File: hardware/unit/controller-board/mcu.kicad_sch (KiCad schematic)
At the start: 26 parts, among them U11 LP2985-33, U12 TPS3823A-33, U13 74LVC1G74, U14 74LVC1G27, U15 74LVC1G02

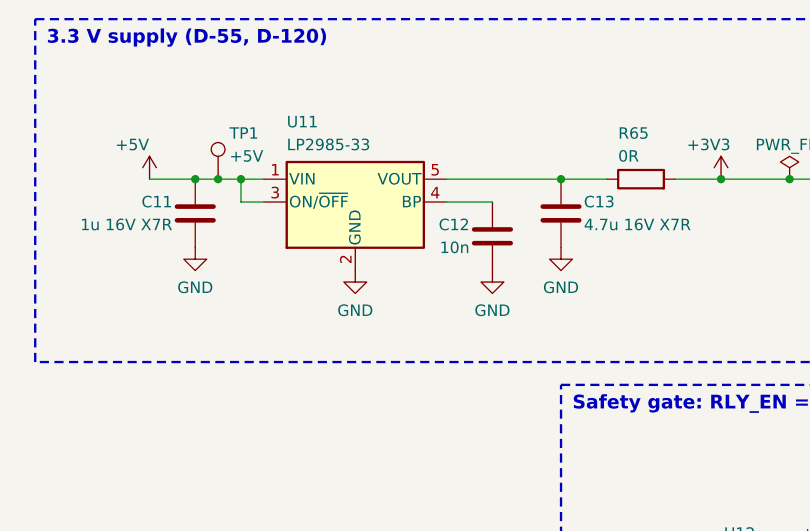
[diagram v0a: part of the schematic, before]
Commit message: Pre-order review; RF board seat keep-outs; part reuse P-1 to P-5
- docs/reviews/2026-10-31-pre-order-review.md: review of all three boards
  before ordering (verify scripts, ERC/DRC, pin maps, BOM, fab and case,
  firmware against spec, open items, part reuse).
- RF board (D-189, M-107): no other-net copper or vias under the case
  seats at S1 to S6 and the SO-239/SMA GND bosses; relay NC pads (pad 12)
  in netclass RF. Re-routed, DRC 0.
- Part reuse (D-190, M-108): one value text for 2k2, 100n 50V X7R and
  10n 50V X7R; shack PC817X order code as the controller; shack U4/U9 in
  VSSOP-8 (TI DCU, Nexperia DC) with fixed fan-out, re-routed.
  Netlists rf15, ctl15, si17; ERC 0.

Co-Authored-By: Claude Opus 5.5 <noreply@anthropic.com>
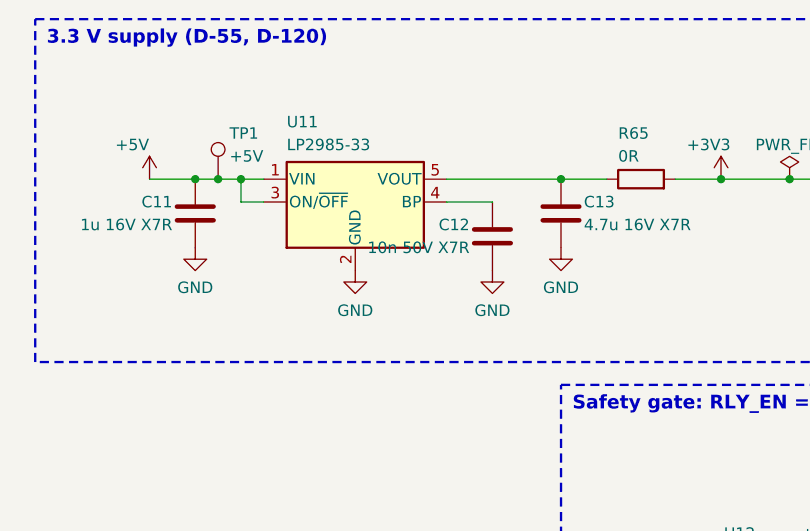
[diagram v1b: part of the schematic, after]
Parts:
- C12: value 10n -> 10n 50V X7R
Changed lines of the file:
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@@
 			)
 		)
-		(property "Value" "10n"
+		(property "Value" "10n 50V X7R"
 			(at 73.66 50.8 0)
 			(show_name no)

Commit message: S-1: FAULT to GPIO6, box fault 11, host clearfault
Hardware (D-191, M-109):
- Controller board: R66 1k from FAULT (U13 Q) to DevKit pin 11 (GPIO6).
  Schematic c15-fault-io6, netlist ctl16, layout c-s6, re-routed.
  ERC 0, DRC 0 violations and 0 unconnected. BOM: R66 on the 1k line.
- gen_controller_pcb.py splits a track where a same-net track ends on it.
- verify_logic.py checks R66 and FAULT_IO6.

Firmware:
- Box reads FAULT. After the self-test, FAULT = 1 gives fault 11
  (supervisor trip); READY stays open.
- New link command ClearFault (0x03): one LATCH_CLR edge, Ok if FAULT
  clears, else NotReady. No edge without a trip.
- Host clearfault also sends ClearFault when the box reports fault 11.
- Sim model, box target (GPIO6), 3 new tests.

Co-Authored-By: Claude Opus 5.5 <noreply@anthropic.com>
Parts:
- added R66: 1k, Resistor_SMD:R_0603_1608Metric_Pad0.98x0.95mm_HandSolder, symbol Device:R
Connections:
- net FAULT: now also R66.1
- net FAULT_IO6: now reaches A1.11 (IO6)
- net FAULT_IO6: now also R66.2
- no-connect marks 17 -> 16
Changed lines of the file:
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@@
 	)
 	(junction
+		(at 160.02 101.6)
+		(diameter 0)
+		(color 0 0 0 0)
+	)
+	(junction
 		(at 142.24 121.92)
 		(diameter 0)
@@
 		)
 	)
-	(no_connect
-		(at 43.18 190.5)
+	(wire
+		(pts
+			(xy 43.18 190.5) (xy 35.56 190.5)
+		)
+		(stroke
+			(width 0)
+			(type default)
+		)
+	)
+	(label "FAULT_IO6"
+		(at 35.56 190.5 180)
+		(effects
+			(font
+				(size 1.27 1.27)
+			)
+			(justify right bottom)
+		)
 	)
 	(wire
@@
 	(wire
 		(pts
-			(xy 160.02 93.98) (xy 160.02 119.38)
+			(xy 160.02 93.98) (xy 160.02 101.6)
+		)
+		(stroke
+			(width 0)
+			(type default)
+		)
+	)
+	(wire
+		(pts
+			(xy 160.02 101.6) (xy 160.02 119.38)
 		)
 		(stroke
@@
 	)
 	(symbol
+		(lib_id "Device:R")
+		(at 167.64 101.6 90)
+		(unit 1)
+		(body_style 1)
+		(exclude_from_sim no)
+		(in_bom yes)
+		(on_board yes)
+		(in_pos_files yes)
+		(dnp no)
+		(property "Reference" "R66"
+			(at 167.64 99.06 270)
+			(show_name no)
+			(do_not_autoplace no)
+			(effects
+				(font
+					(size 1.27 1.27)
+				)
+				(justify left)
+			)
+		)
+		(property "Value" "1k"
+			(at 167.64 101.6 270)
+			(show_name no)
+			(do_not_autoplace no)
+			(effects
+				(font
+					(size 1.27 1.27)
+				)
+				(justify left)
+			)
+		)
+		(property "Footprint" "Resistor_SMD:R_0603_1608Metric_Pad0.98x0.95mm_HandSolder"
+			(at 167.64 101.6 0)
+			(hide yes)
+			(show_name no)
+			(do_not_autoplace no)
+			(effects
+				(font
+					(size 1.27 1.27)
+				)
+				(justify left)
+			)
+		)
+		(property "Datasheet" ""
+			(at 167.64 101.6 0)
+			(hide yes)
+			(show_name no)
+			(do_not_autoplace no)
+			(effects
+				(font
+					(size 1.27 1.27)
+				)
+				(justify left)
+			)
+		)
+		(property "Description" "FAULT to GPIO6 (D-191): series resistor, the MCU reads the fault latch"
+			(at 167.64 101.6 0)
+			(hide yes)
+			(show_name no)
+			(do_not_autoplace no)
+			(effects
+				(font
+					(size 1.27 1.27)
+				)
+				(justify left)
+			)
+		)
+		(pin "1"
+		)
+		(pin "2"
+		)
+		(instances
+			(project "controller-board"
+				(path "/b86ecb39-90cb-58dd-93b8-afa48d7a2239/6efcfdd3-b192-5236-8b01-1f2c86853060"
+					(reference "R66")
+					(unit 1)
+				)
+			)
+		)
+	)
+	(wire
+		(pts
+			(xy 160.02 101.6) (xy 163.83 101.6)
+		)
+		(stroke
+			(width 0)
+			(type default)
+		)
+	)
+	(wire
+		(pts
+			(xy 171.45 101.6) (xy 177.8 101.6)
+		)
+		(stroke
+			(width 0)
+			(type default)
+		)
+	)
+	(label "FAULT_IO6"
+		(at 177.8 101.6 0)
+		(effects
+			(font
+				(size 1.27 1.27)
+			)
+			(justify left bottom)
+		)
+	)
+	(symbol
 		(lib_id "Connector:TestPoint")
 		(at 165.1 93.98 0)
@@
 		)
 	)
-	(text "MCU: ESP32-C3 Rust board A1 (DevKit-RUST-1 Rev 1.2a fitted, RUST-2 fits) in gold socket headers (D-93 to D-95). Net labels at the DevKit pins.\n3V3 pin from U11 (LDO); EN low keeps the board buck off;\n5V/VBUS not connected, so the PC can stay on USB (board diode D6). Wi-Fi and BLE off in firmware.\nI2C: board bus SDA GPIO10 (RUST-1) or GPIO7 (RUST-2), set by JP11 (2-3 or 2-1, D-94); SCL GPIO8. 10k on the board; 2.2k on the RF board.\nGPIO0 EXP_INT, GPIO1 WDI (kick at least every 0.9 s), GPIO3 LATCH_CLR (rising edge), GPIO4 MCU_EN_N (low = relays allowed),\nGPIO5 KILL (read), GPIO20/21 UART 9600 baud. GPIO2, 8, 9 are strapping pins: GPIO2 and GPIO9 not used; GPIO8 is SCL. GPIO6 spare.\nBoard LED on GPIO7 (RUST-1) or GPIO10 (RUST-2): the SDA pin of the other board.\nSafety gate (D-59): RLY_EN = NOR(KILL, MCU_EN_N, FAULT). FAULT is set by RESET_N: power-up, 3V3 below 2.83 to 3.00 V, or no WDI edge for 0.9 to 2.5 s.\nAfter a reset the relays stay off until the MCU gives a LATCH_CLR edge. KILL is not latched. RLY_EN has a 100k pull-down on the RF board.\nREADY_ON = NOR(MCU_EN_N, FAULT) (U15, D-62): closes the READY switch in the SAFE loop. Start-up: LATCH_CLR, MCU_EN_N low, then KILL reads 0 (F11).\nU12 RESET_N does not reset the MCU (DevKit pin 1 RST open); the ESP32-C3 has its own watchdogs. MR open: internal 90k pull-up."
+	(text "MCU: ESP32-C3 Rust board A1 (DevKit-RUST-1 Rev 1.2a fitted, RUST-2 fits) in gold socket headers (D-93 to D-95). Net labels at the DevKit pins.\n3V3 pin from U11 (LDO); EN low keeps the board buck off;\n5V/VBUS not connected, so the PC can stay on USB (board diode D6). Wi-Fi and BLE off in firmware.\nI2C: board bus SDA GPIO10 (RUST-1) or GPIO7 (RUST-2), set by JP11 (2-3 or 2-1, D-94); SCL GPIO8. 10k on the board; 2.2k on the RF board.\nGPIO0 EXP_INT, GPIO1 WDI (kick at least every 0.9 s), GPIO3 LATCH_CLR (rising edge), GPIO4 MCU_EN_N (low = relays allowed),\nGPIO5 KILL (read), GPIO6 FAULT (read, 1k R66, D-191), GPIO20/21 UART 9600 baud. GPIO2, 8, 9 are strapping pins: GPIO2 and GPIO9 not used; GPIO8 is SCL.\nBoard LED on GPIO7 (RUST-1) or GPIO10 (RUST-2): the SDA pin of the other board.\nSafety gate (D-59): RLY_EN = NOR(KILL, MCU_EN_N, FAULT). FAULT is set by RESET_N: power-up, 3V3 below 2.83 to 3.00 V, or no WDI edge for 0.9 to 2.5 s.\nAfter a reset the relays stay off until the MCU gives a LATCH_CLR edge. KILL is not latched. RLY_EN has a 100k pull-down on the RF board.\nREADY_ON = NOR(MCU_EN_N, FAULT) (U15, D-62): closes the READY switch in the SAFE loop. Start-up: LATCH_CLR, MCU_EN_N low, then KILL reads 0 (F11).\nU12 RESET_N does not reset the MCU (DevKit pin 1 RST open); the ESP32-C3 has its own watchdogs. MR open: internal 90k pull-up."
 		(exclude_from_sim no)
 		(at 25.4 223.52 0)

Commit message: S-2: SDA jumpers bridged 1-2 for RUST-1 by default
JP11 (controller) and JP61 (shack) use the Bridged12 solder jumper.
Pad 1 = SDA_IO10 (RUST-1), pad 3 = SDA_IO7 (RUST-2). Boards ship ready
for RUST-1; for RUST-2 cut 1-2 and bridge 2-3. New netlists ctl17 and
si18, new JP11/JP61 checks, boards re-routed, DRC clean. D-192, M-110.

Co-Authored-By: Claude Opus 5.5 <noreply@anthropic.com>
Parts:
- JP11: footprint Jumper:SolderJumper-3_P1.3mm_Open_RoundedPad1.0x1.5mm_NumberLabels -> Jumper:SolderJumper-3_P1.3mm_Bridged12_RoundedPad1.0x1.5mm_NumberLabels; symbol controller-board:SolderJumper_3_Open -> controller-board:SolderJumper_3_Bridged12
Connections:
- net SDA_IO10: now also JP11.1; no longer JP11.3
- net SDA_IO7: now also JP11.3; no longer JP11.1
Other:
- note added: "MCU: ESP32-C3 Rust board A1 (DevKit-RUST-1 Rev 1.2a fitted, RUST-2 fits) in gold socket headers (D-93 to D-95). Net labels at the DevKit pins. 3V3 pin from U11 (LDO); EN low keeps the board buck off; 5V/VBUS not connected, so the PC can stay on USB (board diode D6). Wi-Fi and BLE off in firmware. I2C: board bus SDA GPIO10 (RUST-1) or GPIO7 (RUST-2), set by JP11 (1-2 bridged by copper for RUST-1; 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"
- note removed: "MCU: ESP32-C3 Rust board A1 (DevKit-RUST-1 Rev 1.2a fitted, RUST-2 fits) in gold socket headers (D-93 to D-95). Net labels at the DevKit pins. 3V3 pin from U11 (LDO); EN low keeps the board buck off; 5V/VBUS not connected, so the PC can stay on USB (board diode D6). Wi-Fi and BLE off in firmware. I2C: board bus SDA GPIO10 (RUST-1) or GPIO7 (RUST-2), set by JP11 (2-3 or 2-1, D-94); SCL GPIO8. 10k 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"
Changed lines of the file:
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@@
 			)
 		)
-		(property "Description" "ESP32-C3 Rust board pushed into gold-flash socket headers Sullins PPPC161LFBN-RC (1x16) and PPPC121LFBN-RC (1x12) (D-55, D-93 to D-95). RUST-1 Rev 1.2a fitted; RUST-2 fits with JP11 2-1"
+		(property "Description" "ESP32-C3 Rust board pushed into gold-flash socket headers Sullins PPPC161LFBN-RC (1x16) and PPPC121LFBN-RC (1x12) (D-55, D-93 to D-95). RUST-1 Rev 1.2a fitted; RUST-2 fits with JP11 1-2 cut and 2-3 bridged"
 			(at 60.96 182.88 0)
 			(hide yes)
@@
 	)
 	(symbol
-		(lib_id "controller-board:SolderJumper_3_Open")
+		(lib_id "controller-board:SolderJumper_3_Bridged12")
 		(at 48.26 129.54 90)
 		(unit 1)
@@
 			)
 		)
-		(property "Footprint" "Jumper:SolderJumper-3_P1.3mm_Open_RoundedPad1.0x1.5mm_NumberLabels"
+		(property "Footprint" "Jumper:SolderJumper-3_P1.3mm_Bridged12_RoundedPad1.0x1.5mm_NumberLabels"
 			(at 48.26 129.54 0)
 			(hide yes)
@@
 			)
 		)
-		(property "Description" "SDA select (D-94): bridge 2-3 for DevKit-RUST-1 (SDA GPIO10, pad 17), 2-1 for DevKit-RUST-2 (SDA GPIO7, pad 12). Firmware SDA pin must match"
+		(property "Description" "SDA select (D-94, D-192): 1-2 bridged by copper = DevKit-RUST-1 (SDA GPIO10, pad 17). DevKit-RUST-2 (SDA GPIO7, pad 12): cut 1-2, bridge 2-3. Firmware SDA pin must match"
 			(at 48.26 129.54 0)
 			(hide yes)
@@
 		)
 	)
-	(label "SDA_IO7"
+	(label "SDA_IO10"
 		(at 48.26 142.24 270)
 		(effects
@@
 		)
 	)
-	(label "SDA_IO10"
+	(label "SDA_IO7"
 		(at 48.26 116.84 90)
 		(effects
@@
 		)
 	)
-	(text "MCU: ESP32-C3 Rust board A1 (DevKit-RUST-1 Rev 1.2a fitted, RUST-2 fits) in gold socket headers (D-93 to D-95). Net labels at the DevKit pins.\n3V3 pin from U11 (LDO); EN low keeps the board buck off;\n5V/VBUS not connected, so the PC can stay on USB (board diode D6). Wi-Fi and BLE off in firmware.\nI2C: board bus SDA GPIO10 (RUST-1) or GPIO7 (RUST-2), set by JP11 (2-3 or 2-1, D-94); SCL GPIO8. 10k on the board; 2.2k on the RF board.\nGPIO0 EXP_INT, GPIO1 WDI (kick at least every 0.9 s), GPIO3 LATCH_CLR (rising edge), GPIO4 MCU_EN_N (low = relays allowed),\nGPIO5 KILL (read), GPIO6 FAULT (read, 1k R66, D-191), GPIO20/21 UART 9600 baud. GPIO2, 8, 9 are strapping pins: GPIO2 and GPIO9 not used; GPIO8 is SCL.\nBoard LED on GPIO7 (RUST-1) or GPIO10 (RUST-2): the SDA pin of the other board.\nSafety gate (D-59): RLY_EN = NOR(KILL, MCU_EN_N, FAULT). FAULT is set by RESET_N: power-up, 3V3 below 2.83 to 3.00 V, or no WDI edge for 0.9 to 2.5 s.\nAfter a reset the relays stay off until the MCU gives a LATCH_CLR edge. KILL is not latched. RLY_EN has a 100k pull-down on the RF board.\nREADY_ON = NOR(MCU_EN_N, FAULT) (U15, D-62): closes the READY switch in the SAFE loop. Start-up: LATCH_CLR, MCU_EN_N low, then KILL reads 0 (F11).\nU12 RESET_N does not reset the MCU (DevKit pin 1 RST open); the ESP32-C3 has its own watchdogs. MR open: internal 90k pull-up."
+	(text "MCU: ESP32-C3 Rust board A1 (DevKit-RUST-1 Rev 1.2a fitted, RUST-2 fits) in gold socket headers (D-93 to D-95). Net labels at the DevKit pins.\n3V3 pin from U11 (LDO); EN low keeps the board buck off;\n5V/VBUS not connected, so the PC can stay on USB (board diode D6). Wi-Fi and BLE off in firmware.\nI2C: board bus SDA GPIO10 (RUST-1) or GPIO7 (RUST-2), set by JP11 (1-2 bridged by copper for RUST-1; RUST-2: cut 1-2, bridge 2-3; D-94, D-192); SCL GPIO8. 10k on the board; 2.2k on the RF board.\nGPIO0 EXP_INT, GPIO1 WDI (kick at least every 0.9 s), GPIO3 LATCH_CLR (rising edge), GPIO4 MCU_EN_N (low = relays allowed),\nGPIO5 KILL (read), GPIO6 FAULT (read, 1k R66, D-191), GPIO20/21 UART 9600 baud. GPIO2, 8, 9 are strapping pins: GPIO2 and GPIO9 not used; GPIO8 is SCL.\nBoard LED on GPIO7 (RUST-1) or GPIO10 (RUST-2): the SDA pin of the other board.\nSafety gate (D-59): RLY_EN = NOR(KILL, MCU_EN_N, FAULT). FAULT is set by RESET_N: power-up, 3V3 below 2.83 to 3.00 V, or no WDI edge for 0.9 to 2.5 s.\nAfter a reset the relays stay off until the MCU gives a LATCH_CLR edge. KILL is not latched. RLY_EN has a 100k pull-down on the RF board.\nREADY_ON = NOR(MCU_EN_N, FAULT) (U15, D-62): closes the READY switch in the SAFE loop. Start-up: LATCH_CLR, MCU_EN_N low, then KILL reads 0 (F11).\nU12 RESET_N does not reset the MCU (DevKit pin 1 RST open); the ESP32-C3 has its own watchdogs. MR open: internal 90k pull-up."
 		(exclude_from_sim no)
 		(at 25.4 223.52 0)

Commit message: S-10: MAX823SEUK+T first source, IRFL9014TRPBF-BE3 (D-195, M-118)
Supervisor U12 (controller), U3 and U6 (shack): MAX823SEUK+T first,
TPS3823A-33DBVR and APX823-29W5G-7 second. Same pin-out; RESET_N loads
are CMOS inputs; WDI and MR behave as the TPS3823 in our circuits.
RF Q1012 to Q1042: IRFL9014TRPBF-BE3. TLP176AM in stock at Mouser.
SO-239 83-798 stays single source, order first. Values and boards
unchanged. ERC 0 on all three.

Co-Authored-By: Claude Opus 5.5 <noreply@anthropic.com>
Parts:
- U12: MPN TPS3823A-33DBVR -> MAX823SEUK+T
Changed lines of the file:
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@@
 			)
 		)
-		(property "Description" "Supervisor 2.93 V + watchdog 0.9 to 2.5 s, push-pull RESET_N, -40 to 125 C (TI SLVS165O). A version: no latch-up on WDI pulses during reset"
+		(property "Description" "Supervisor 2.93 V (2.85 to 3.00) + watchdog 1.12 to 2.4 s, push-pull RESET_N (150 uA source: logic loads only), -40 to 125 C (ADI MAX823 19-0487 Rev 5). Second sources TI TPS3823A-33DBVR (A version only: no latch-up on WDI pulses during reset) and Diodes APX823-29W5G-7 (D-148, D-195)"
 			(at 114.3 93.98 0)
 			(hide yes)
@@
 			)
 		)
-		(property "MPN" "TPS3823A-33DBVR"
+		(property "MPN" "MAX823SEUK+T"
 			(at 114.3 93.98 0)
 			(hide yes)
@@
 			)
 		)
-		(property "Description" "Watchdog link (D-123): fitted in use. Open on the bench: U12 WDI floats, so the watchdog is off (TPS3823 SLVS165O 7.3.4); the supply supervisor stays active"
+		(property "Description" "Watchdog link (D-123): fitted in use. Open on the bench: U12 WDI floats, so the watchdog is off (MAX823 WDI pin; TPS3823 SLVS165O 7.3.4); the supply supervisor stays active"
 			(at 100.33 91.44 0)
 			(hide yes)
@@
 			)
 		)
-		(property "Description" "WDI pull-down: a floating WDI would disable the watchdog (TPS3823 datasheet 7.3.4)"
+		(property "Description" "WDI pull-down: a floating WDI would disable the watchdog (MAX823 WDI pin; TPS3823 7.3.4). MAX823 WDI sources max 20 uA: 20 mV low"
 			(at 96.52 95.25 0)
 			(hide yes)
